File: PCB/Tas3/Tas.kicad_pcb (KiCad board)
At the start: 2 copper layers, 14 x 28 mm, 24 parts, among them J1 Shelly 1, J2 Conn_01x07, J3 USB-C, U1 MD8942, U3 CH340X, U4 ZXGD3009E6, U5 ZXGD3009E6

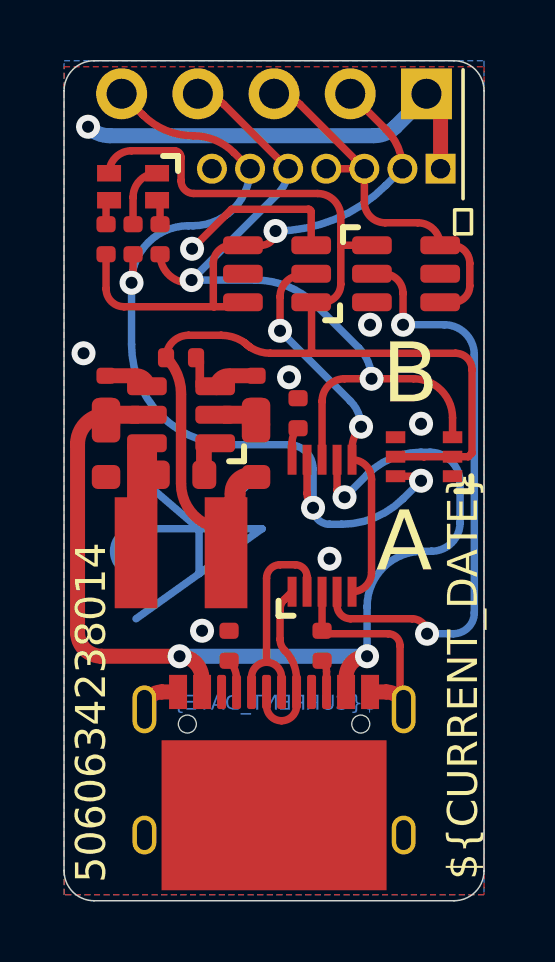
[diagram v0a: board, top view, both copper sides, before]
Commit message: Swapped connector around
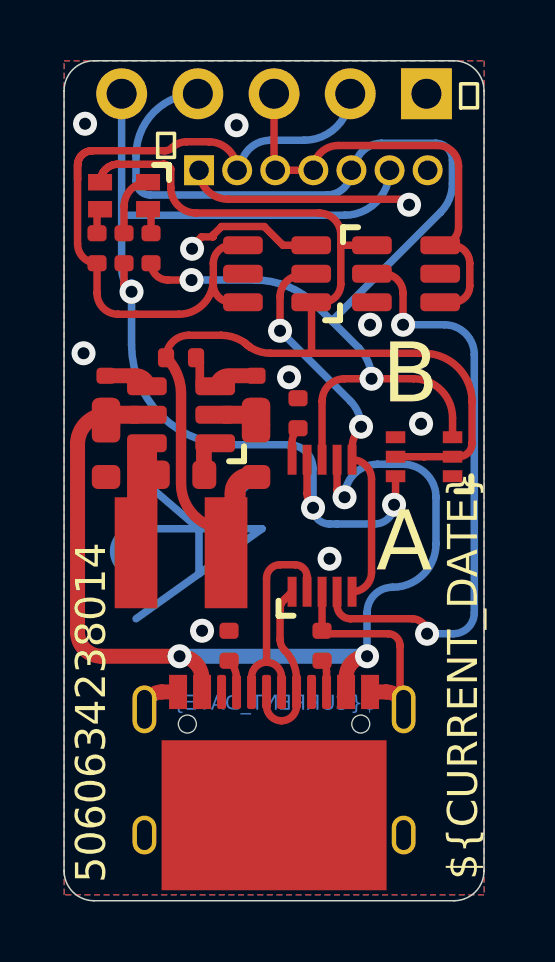
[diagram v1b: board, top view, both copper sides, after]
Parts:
- moved J2 0.43 mm to (100.3, 44.6), turned to 90 degrees
- moved R13 0.42 mm to (93.1, 47.2)
- moved D5 0.42 mm to (94.0, 45.5)
- moved R11 0.42 mm to (94.0, 47.2)
- moved R12 0.42 mm to (94.9, 47.2)
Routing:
- net G: track 26.1 -> 40.1 mm
- net GND: track 28.4 -> 21.0 mm, vias 8 -> 10
- net B: track 17.6 -> 24.8 mm, vias 1 -> 0
- net R: track 30.6 -> 35.1 mm
- net RST+: track 12.2 -> 14.9 mm
- net VBUS: track 34.8 -> 33.1 mm
- net +3V8: track 32.2 -> 31.2 mm

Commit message: Try again, as ordered.
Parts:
- removed U5: ZXGD3009E6, RevK:SOT-23-6
- added Q1: AP2003, RevK:SOT-23-6, F.Cu at (102.8, 48.0)
- added U2: 74LVC1G07, RevK:SOT-353_SC-70-5, F.Cu at (99.6, 47.8)
- R4: value 34k4 -> 39k2
- U4: value ZXGD3009E6 -> 74LVC1G06SE-7; footprint RevK:SOT-23-6 -> RevK:SOT-353_SC-70-5
- moved U4 11.1 mm to (104.2, 58.0), turned to 90 degrees
- moved D5 1.65 mm to (94.0, 47.1)
- moved R11 1.65 mm to (94.0, 48.9)
- moved R12 1.65 mm to (94.9, 48.9)
- moved R13 1.65 mm to (93.1, 48.9)
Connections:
- C5 pad 1: Net-(U3-V3) -> +3V3
- D1 pad 2: +3V8 -> +3V3
- D1 pad 5: +3V8 -> +3V3
- D5 pad 4: +3V8 -> +3V3
- J2 pad 4: RST+ -> +3V3
- U1 pad 8: +3V8 -> +3V3
- U3 pad 10: Net-(U3-V3) -> +3V3
- U3 pad 7: VBUS -> +3V3
- U4 pad 1: +3V8 -> unconnected-(U4-NC-Pad1)
- U4 pad 2: GPIO0 -> RST
- U4 pad 4: B -> Net-(Q1A-G)
- U4 pad 5: unconnected-(U4-NC-Pad5) -> +3V3
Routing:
- net +3V3: track 0.00 -> 54.7 mm
- net +3V8: track 31.2 -> 0.00 mm
- net RST: track 19.5 -> 4.47 mm, vias 2 -> 0
- net VBUS: track 33.1 -> 21.0 mm, vias 3 -> 2
- net Net-(Q1A-G): track 0.00 -> 11.2 mm, vias 0 -> 2
- net GND: track 21.0 -> 13.4 mm
- net RST+: track 14.9 -> 8.90 mm
- net B: track 24.8 -> 19.3 mm
- net GPIO0: track 12.4 -> 15.2 mm
- net Net-(U3-V3): track 1.10 -> 0.00 mm
- net R: track 35.1 -> 34.2 mm

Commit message: Maybe Nth time lucky
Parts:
- added C2: 100nF, RevK:C_0402, F.Cu at (99.6, 52.7)
- added R5: 4K7, RevK:R_0402, F.Cu at (105.0, 50.7)
- added R6: 4K7, RevK:R_0402, F.Cu at (93.2, 45.4)
- moved C5 2.80 mm to (100.3, 50.0), turned to 180 degrees
- moved Art1 0.50 mm to (96.5, 56.1)
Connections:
- U3 pad 10: +3V3 -> Net-(U3-V3)
- U3 pad 7: +3V3 -> VBUS
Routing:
- net +3V3: track 54.7 -> 46.9 mm
- net VBUS: track 21.0 -> 28.3 mm, vias 2 -> 3
- net Net-(Q1A-G): track 11.2 -> 12.6 mm
- net Net-(U3-V3): track 0.00 -> 1.10 mm

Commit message: FFS
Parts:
- added C3: 100nF, RevK:C_0402, F.Cu at (101.8, 53.1)
- added C4: 22uF, RevK:C_0402, F.Cu at (101.8, 52.1)
- C2: value 100nF -> 10nF
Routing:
- net G: track 40.1 -> 42.7 mm
- net GND: track 13.4 -> 10.8 mm
- net VBUS: track 28.3 -> 30.6 mm
- net GPIO0: track 15.2 -> 16.1 mm
